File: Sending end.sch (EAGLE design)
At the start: 17 parts, among them IC1 MEGA8-P

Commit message: sending end echematic version 3.0. need more work on the DCDC converter
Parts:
- removed D3, D4, D5: ZPY, diode:ZPY
- removed R1, R10, R3, R4, R5, R6, R7, R8, R9: tbd, resistor:R-EU_M0805
- added C1, C2, C3, C4, C5, C6, C7: (no value), rcl:C-EUC0805
- added R12, R13, R14, R15, R16, R17, R18, R19, R20: tbd, resistor:R-EU_M0805
- added R21: 10k, resistor:R-EU_M0805
- added T1, T2, T3: (no value), zetex:PMOSSOT23
- added TP1, TP10, TP11, TP12, TP13, TP14, TP2, TP3, TP4, TP5, TP6, TP7, TP8, TP9: PTR1PAD1-20, testpad:PTR1PAD1-20
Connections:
- removed net N$10: R5.1, R8.1, R9.1
- removed net N$2: D4.C, IC1.PC1(ADC1), R10.2, R4.2, R7.2
- removed net N$26: D3.C, IC1.PC0(ADC0), R1.2, R3.2, R6.2
- removed net N$3: D5.C, IC1.PC2(ADC2), R5.2, R8.2, R9.2
- removed net N$5: R1.1, R3.1, R6.1
- removed net N$8: R10.1, R4.1, R7.1
- new net LEFT: R17.1
- new net N$12: IC1.PB6(XTAL1/TOSC1), TP1.TP
- new net N$31: C1.2, C6.2
- new net N$34: C4.1, R16.2, R17.2, T2.G
- new net N$35: R15.2, T2.D
- new net N$37: C5.1, R19.2, R20.2, T3.G
- new net N$39: IC1.PB7(XTAL2/TOSC2), TP3.TP
- new net N$40: IC1.PD5(T1), TP8.TP
- new net N$41: IC1.PC3(ADC3), R12.2, T1.D
- new net RIGHT: R14.1
- new net STOP: R20.1
- new net VCC1: C7.1
- net GND: now also C2.2, C3.2, C4.2, C5.2, C7.2, R13.1, R16.1, R19.1, T1.S, T2.S, T3.S; no longer D3.A, D4.A, D5.A, IC1.PB6(XTAL1/TOSC1), IC1.PB7(XTAL2/TOSC2)
- net N$1: now also TP5.TP
- net N$11: now also C3.1, R13.2, R14.2, T1.G; no longer IC1.PC3(ADC3)
- net N$13: now also R18.2, T3.D
- net N$15: now also TP4.TP
- net N$16: now also TP7.TP
- net N$17: now also TP6.TP
- net N$18: now also TP9.TP
- net N$19: now also TP10.TP
- net N$21: now also TP13.TP
- net N$22: now also TP14.TP
- net N$27: now also TP11.TP
- net N$28: now also TP12.TP
- net N$7: now also R21.2
- net VCC: now also C1.1, C6.1, R12.1, R15.1, R18.1, R21.1; no longer IC1.AVCC
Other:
- note added: "Night Rider: Transmission Board"
- note added: "Solomon Cooper Jessie Bates Brandon Valentine Abdullah Al Madan"
- note added: "Version 2.0"
- moved on the sheet: 12V-5VDCDCCONVERTER, D2, JP1, R2

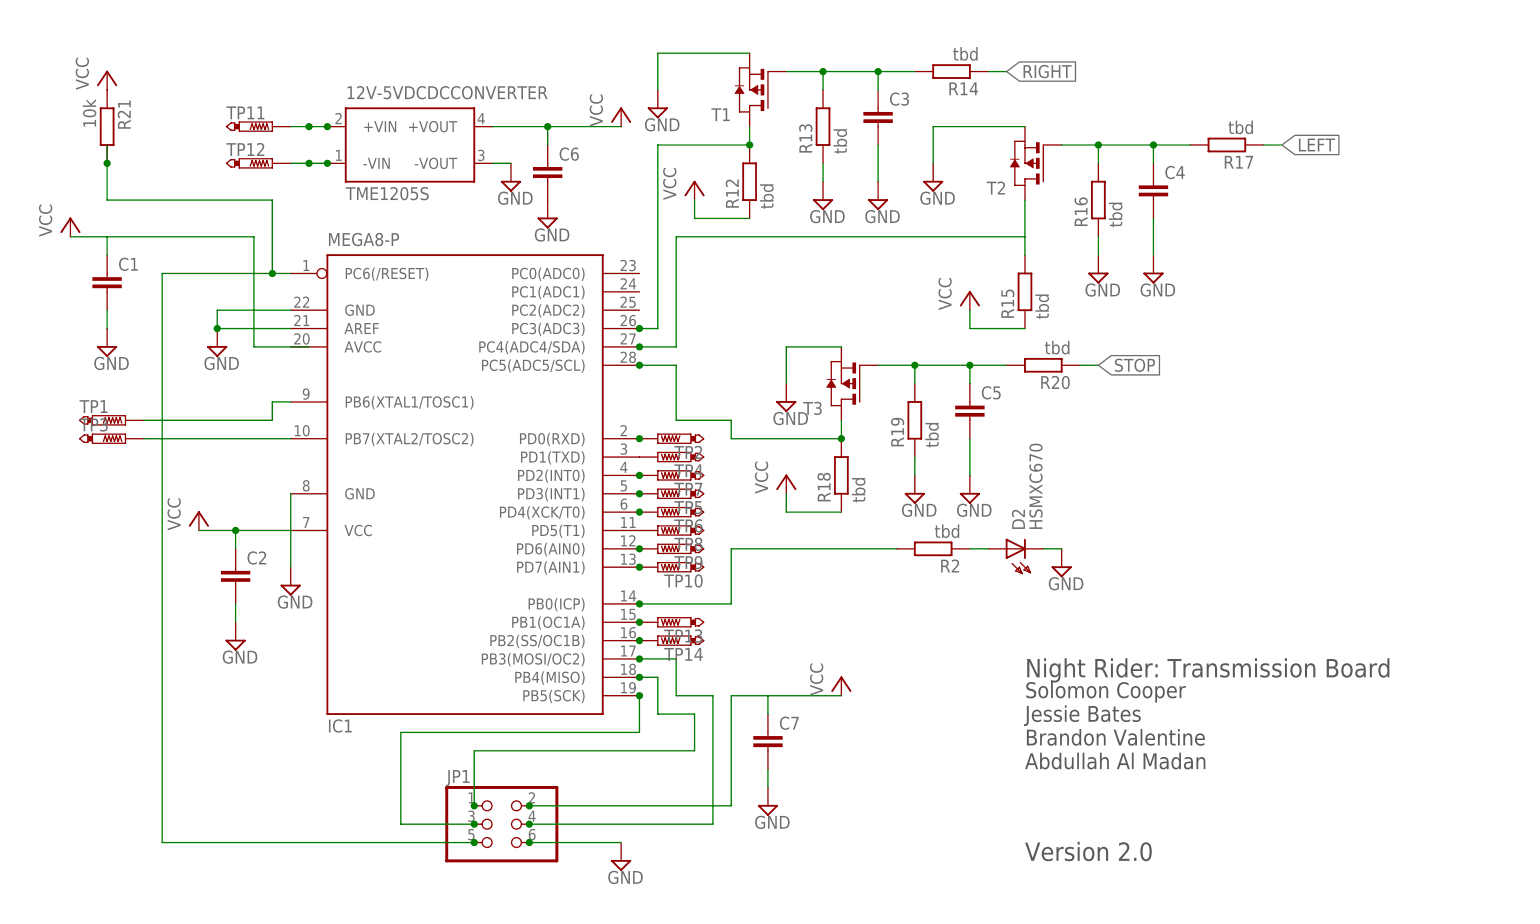
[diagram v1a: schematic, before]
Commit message: the sending end schematic Version 4.0 it has the following modifications: DCtoDCconverter connected as desired; the diode for transmission has an NMOS transistor to amplify the current
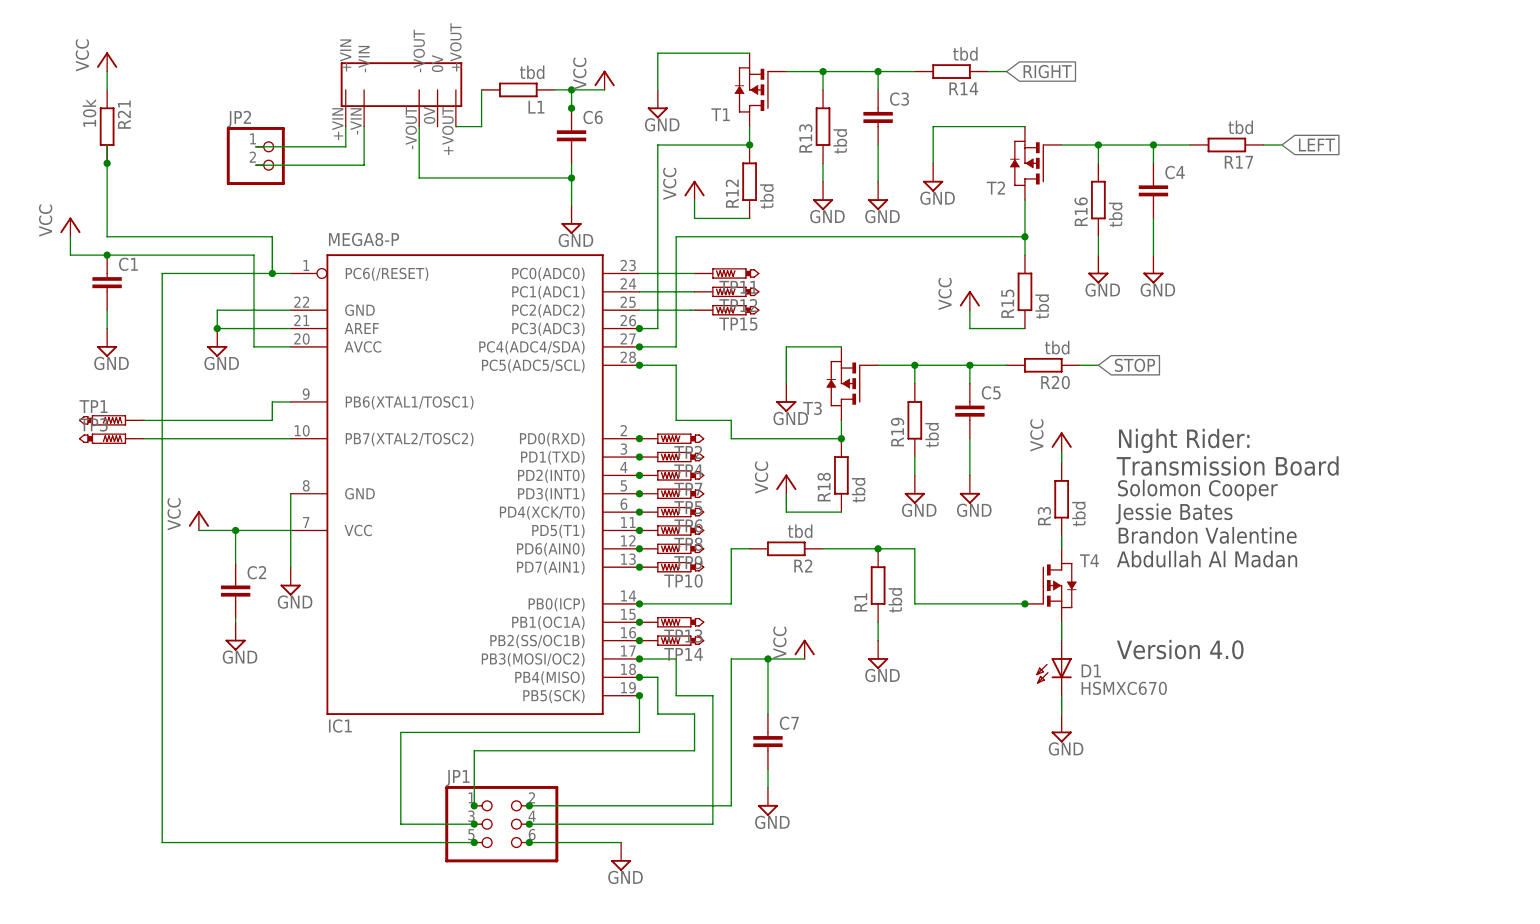
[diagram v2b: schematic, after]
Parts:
- removed 12V-5VDCDCCONVERTER: TME1205S, traco-electronic:TME1205S
- removed D2: HSMXC670, opto-transmittter-hp:HSMXC670
- added D1: HSMXC670, opto-transmittter-hp:HSMXC670
- added JP2: (no value), pinhead:PINHD-1X2
- added L1, R1, R3: tbd, resistor:R-EU_M0805
- added T4: (no value), zetex:PMOSSOT23
- added TP15: PTR1PAD1-20, testpad:PTR1PAD1-20
- added U$1: (no value), nka1205sc:NKA1205SC
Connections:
- removed net N$14: IC1.PD0(RXD)
- removed net N$31: C1.2, C6.2
- removed net N$42: IC1.PC4(ADC4/SDA)
- removed net VCC1: C7.1
- new net N$2: R1.2, R2.1, T4.G
- new net N$26: JP2.2, U$1.-VIN
- new net N$29: IC1.PC2(ADC2), TP15.TP
- new net N$3: R3.1, T4.D
- new net N$30: JP2.1, U$1.+VIN
- new net N$5: IC1.PD0(RXD), TP2.TP
- new net N$8: L1.2, U$1.+VOUT
- net GND: now also C1.2, C6.2, D1.C, R1.1, U$1.-VOUT; no longer 12V-5VDCDCCONVERTER.-VOUT, D2.C
- net N$27: now also IC1.PC0(ADC0); no longer 12V-5VDCDCCONVERTER.+VIN
- net N$28: now also IC1.PC1(ADC1); no longer 12V-5VDCDCCONVERTER.-VIN
- net N$35: now also IC1.PC4(ADC4/SDA)
- net N$6: now also D1.A, T4.S; no longer D2.A, R2.1
- net VCC: now also C2.1, C7.1, IC1.AVCC, L1.1, R3.2; no longer 12V-5VDCDCCONVERTER.+VOUT
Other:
- note added: "Version 4.0"
- note removed: "Version 2.0"
- moved on the sheet: C2, C6, R2, TP11, TP12
